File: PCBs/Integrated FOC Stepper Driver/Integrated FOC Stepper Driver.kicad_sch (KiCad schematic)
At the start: 55 parts, among them J1 USB C Receptacle, J2 Conn_01x03, J3 INPUT, J4 OUTPUT, J5 Conn_01x02, J6 MOTOR, U1 RP2040, U2 W25Q128JVS, U3 PJ54M50SE, U4 PJ9500M33SA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

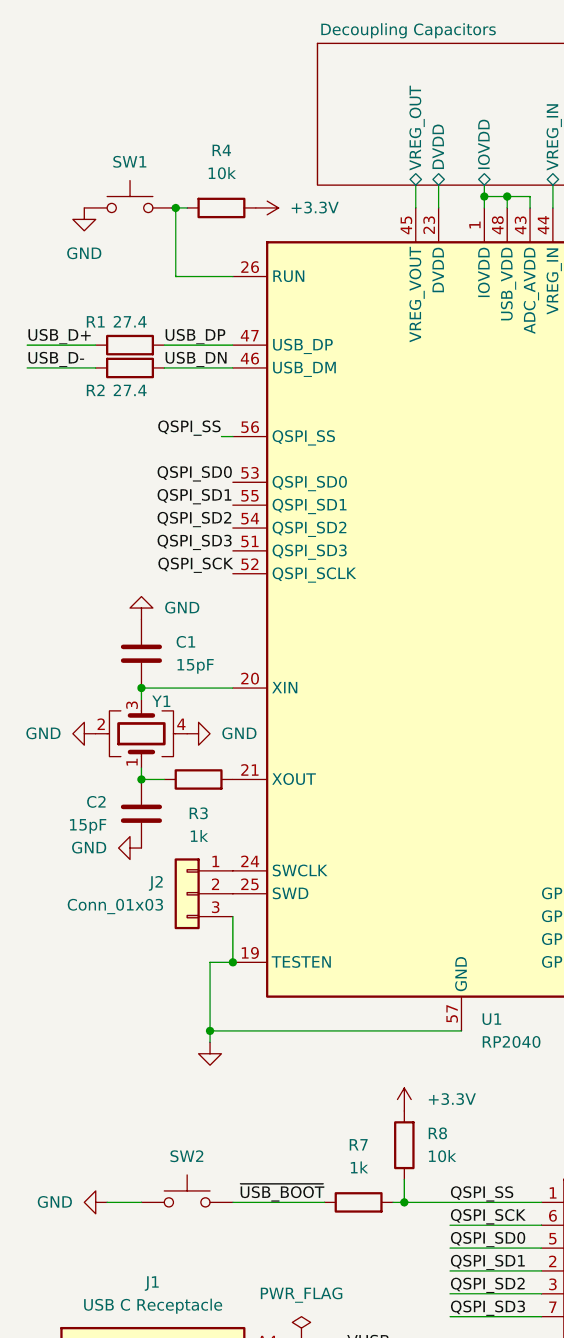
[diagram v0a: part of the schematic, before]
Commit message: Finish new layout
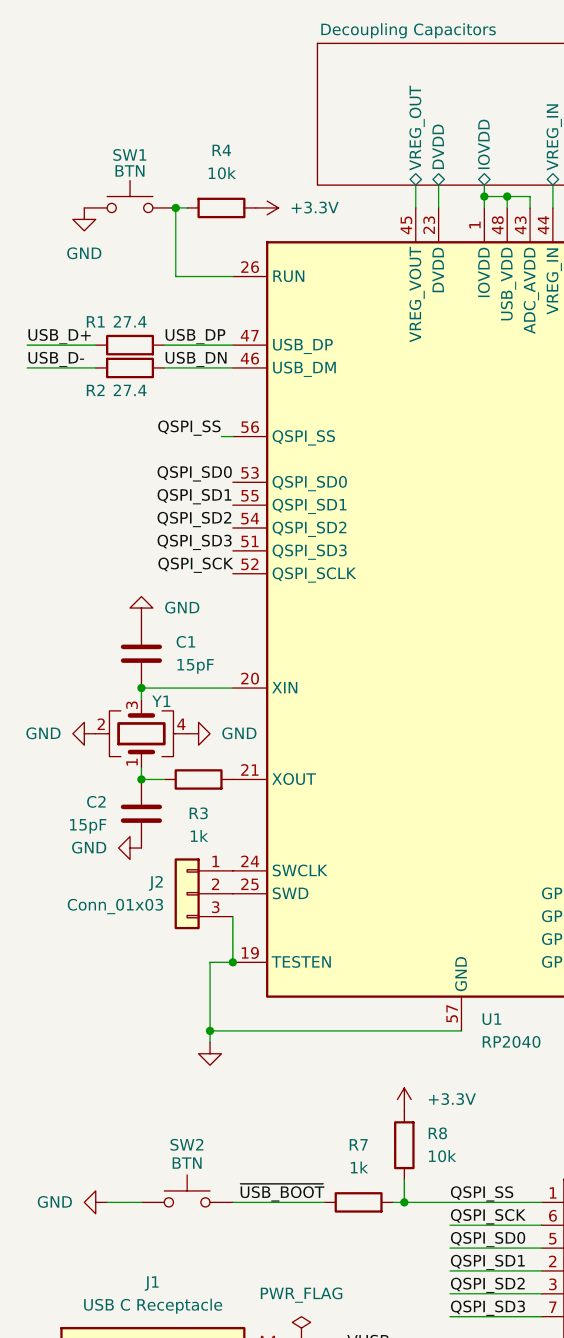
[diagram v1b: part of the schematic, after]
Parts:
- J6: LCSC C2831798 -> C157925
- SW1, SW2: value ~ -> BTN
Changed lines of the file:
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@@
 			)
 		)
-		(property "LCSC" "C2831798"
+		(property "LCSC" "C157925"
 			(at 153.67 30.48 0)
 			(effects
@@
 		(on_board yes)
 		(dnp no)
-		(fields_autoplaced yes)
 		(property "Reference" "SW2"
-			(at 30.48 139.7 0)
+			(at 30.48 138.43 0)
 			(effects
 				(font
@@
 			)
 		)
-		(property "Value" "~"
-			(at 30.48 139.7 0)
+		(property "Value" "BTN"
+			(at 30.48 140.462 0)
 			(effects
 				(font
@@
 		(on_board yes)
 		(dnp no)
-		(fields_autoplaced yes)
 		(property "Reference" "SW1"
-			(at 24.13 29.21 0)
+			(at 24.13 28.448 0)
 			(effects
 				(font
@@
 			)
 		)
-		(property "Value" "~"
-			(at 24.13 29.21 0)
+		(property "Value" "BTN"
+			(at 24.13 30.226 0)
 			(effects
 				(font

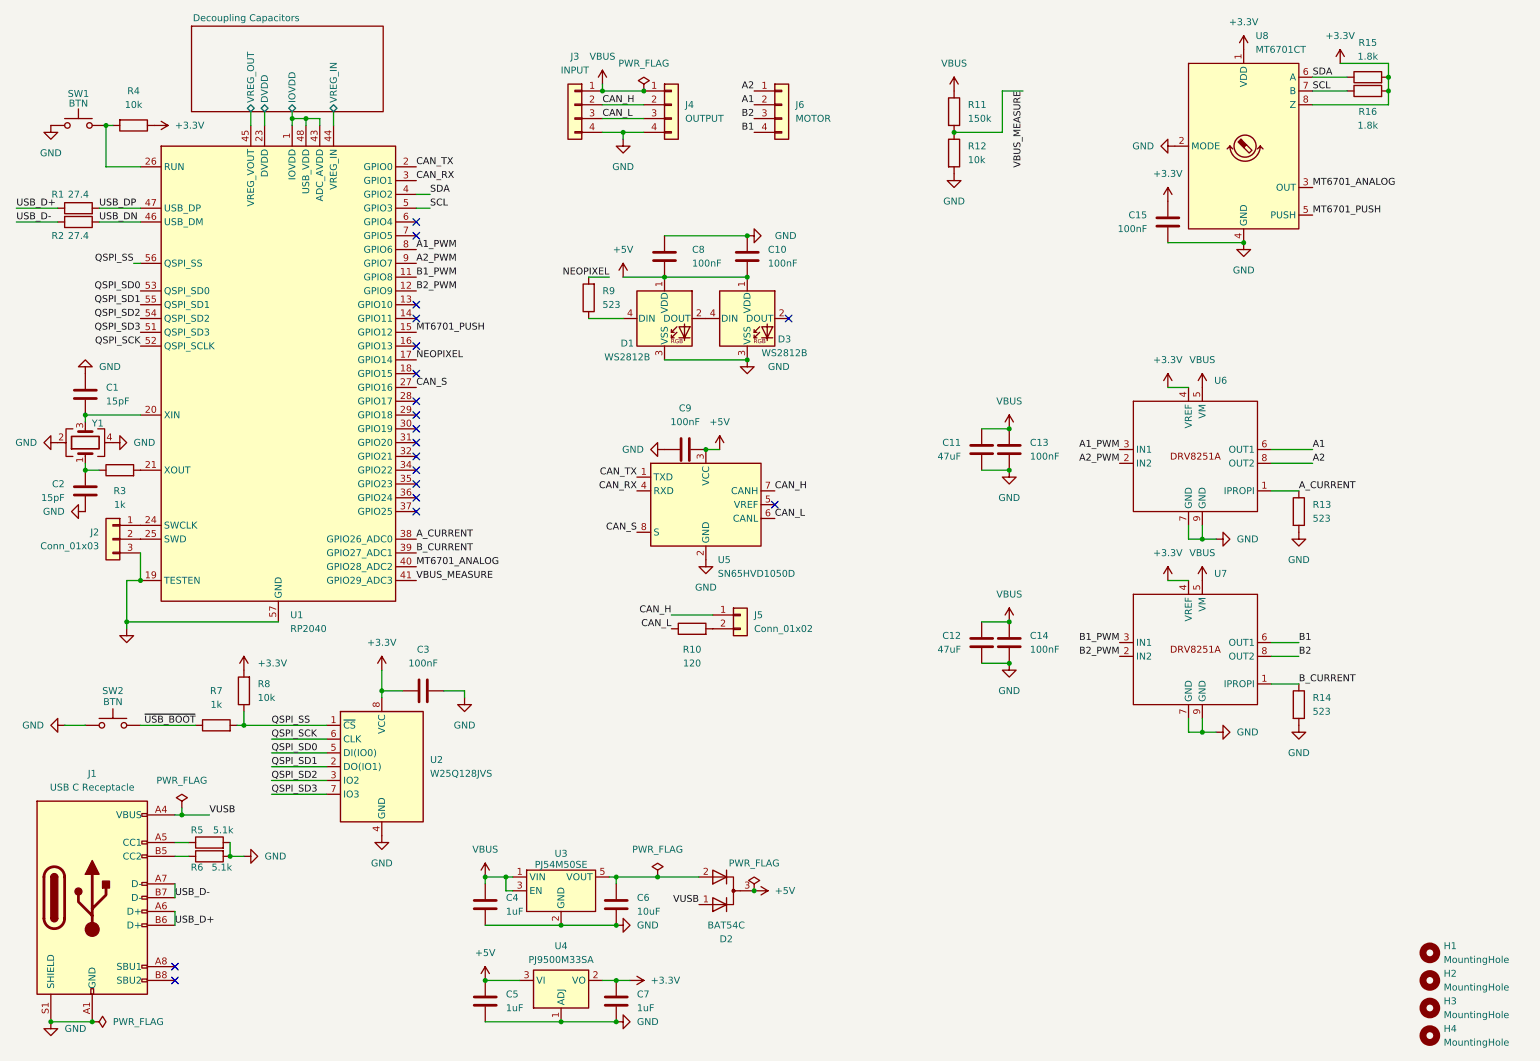
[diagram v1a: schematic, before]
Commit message: Switch to 0805 capacitors instead of stacked 2220 capacitors
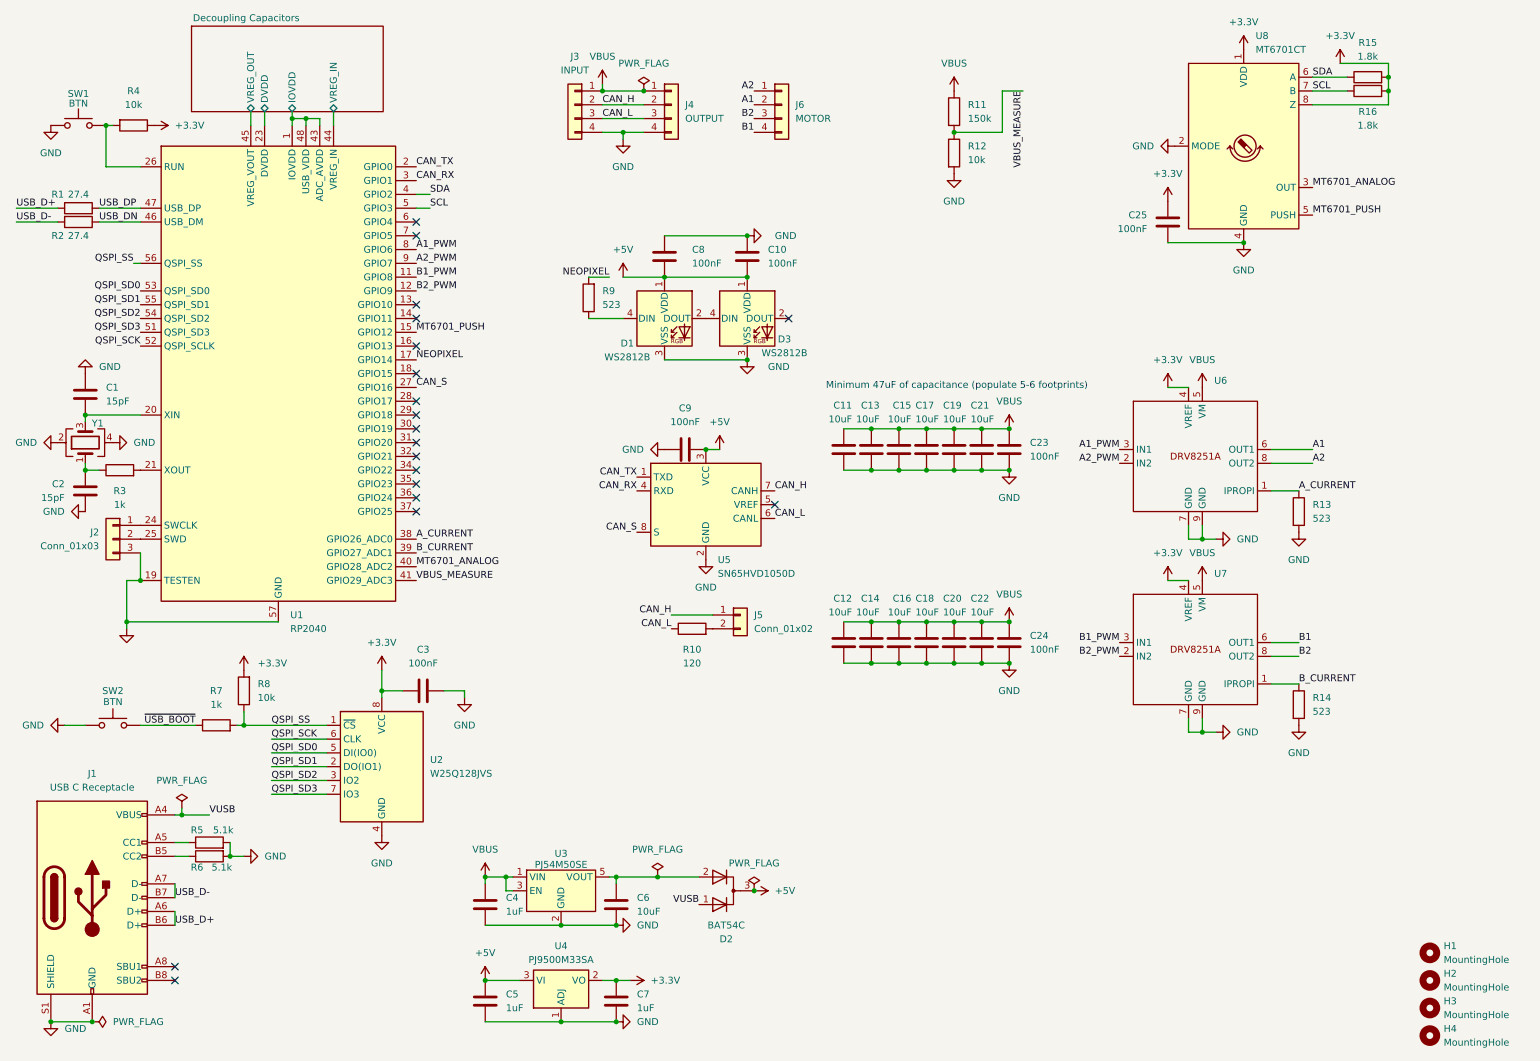
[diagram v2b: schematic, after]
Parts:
- added C11, C13, C14, C15, C16, C17, C18, C19, C20, C22: 10uF, Capacitor_SMD:C_0805_2012Metric, symbol Device:C
- C12: value 47uF -> 10uF; footprint Capacitor_SMD:C_2220_5750Metric -> Capacitor_SMD:C_0805_2012Metric; LCSC C5447693 -> C440198
- C21: renamed from C11; value 47uF -> 10uF; footprint Capacitor_SMD:C_2220_5750Metric -> Capacitor_SMD:C_0805_2012Metric; LCSC C5447693 -> C440198
- renumbered C13 to C23, C14 to C24, C15 to C25
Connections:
- net GND: now also C11.2, C13.2, C14.2, C15.2, C16.2, C17.2, C18.2, C19.2, C20.2, C22.2
- net VBUS: now also C11.1, C13.1, C14.1, C15.1, C16.1, C17.1, C18.1, C19.1, C20.1, C22.1
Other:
- note added: "Minimum 47uF of capacitance (populate 5-6 footprints)"

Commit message: Update bypass capacitors
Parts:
- C25: footprint Capacitor_SMD:C_0402_1005Metric -> Capacitor_SMD:C_0603_1608Metric; LCSC C960916 -> C1591
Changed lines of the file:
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@@
 			)
 		)
-		(property "Footprint" "Capacitor_SMD:C_0402_1005Metric"
+		(property "Footprint" "Capacitor_SMD:C_0603_1608Metric"
 			(at 223.8248 55.88 0)
 			(effects
@@
 			)
 		)
-		(property "LCSC" "C960916"
+		(property "LCSC" "C1591"
 			(at 224.79 52.07 0)
 			(effects

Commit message: new firmware
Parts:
- R15, R16: value 1.8k -> 5.1k
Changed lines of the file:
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@@
 			)
 		)
-		(property "Value" "1.8k"
+		(property "Value" "5.1k"
 			(at 261.62 21.59 90)
 			(effects
@@
 		(on_board yes)
 		(dnp no)
-		(fields_autoplaced yes)
 		(property "Reference" "R16"
 			(at 261.62 31.75 90)
@@
 			)
 		)
-		(property "Value" "1.8k"
+		(property "Value" "5.1k"
 			(at 261.62 34.29 90)
 			(effects
